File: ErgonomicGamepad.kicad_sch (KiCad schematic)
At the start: 82 parts, among them J1 USB_C_Receptacle_USB2.0_16P, J2 Conn_01x08, J3 Conn_01x08, J4 Conn_01x08, J5 AVR-ISP-6, J6 Conn_01x08, J7 1824417, SW01 SW_DIP_x01, SW02 SW_DIP_x01, SW03 SW_DIP_x01, SW04 SW_DIP_x01, SW05 SW_DIP_x01, SW06 SW_DIP_x01, SW07 SW_DIP_x01, SW08 SW_DIP_x01, SW09 SW_DIP_x01, SW10 SW_DIP_x01, SW11 SW_DIP_x01, SW12 SW_DIP_x01, SW13 SW_DIP_x01, SW14 SW_DIP_x01, SW15 SW_DIP_x01, SW16 SW_DIP_x01, SW17 SW_DIP_x01, SW18 SW_DIP_x01, SW19 SW_DIP_x01, SW20 SW_DIP_x01, SW21 SW_DIP_x01, SW22 SW_DIP_x01, SW23 SW_DIP_x01, SW24 SW_DIP_x01, U1 ATmega32U4-A, U2 USBLC6-2SC6, Y1 Crystal

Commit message: schematic+pcb: mark JP1/TP1-TP7 as DNP and not real parts
JP1 (solder jumper) and TP1-TP7 (test points) are bare PCB pads, not
sourced components, so mark them Do Not Populate and excluded from
BOM, and drop the empty Datasheet field (Manufacturer/MPN/Supplier/
LCSC were never set on these). PCB updated from schematic to match.

Co-Authored-By: Claude Sonnet 5 <noreply@anthropic.com>
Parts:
- JP1: now not fitted
- TP1, TP2, TP3, TP4, TP5, TP6, TP7: now not fitted; now left out of the parts list
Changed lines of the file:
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@@
 		(on_board yes)
 		(in_pos_files yes)
-		(dnp no)
+		(dnp yes)
 		(fields_autoplaced yes)
 		(property "Reference" "JP1"
@@
 			)
 		)
-		(property "Datasheet" ""
-			(at 62.23 52.07 0)
-			(hide yes)
-			(show_name no)
-			(do_not_autoplace no)
-			(effects
-				(font
-					(size 1.27 1.27)
-				)
-			)
-		)
 		(property "Description" "Solder Jumper, 2-pole, open"
 			(at 59.69 52.07 0)
@@
 		(body_style 1)
 		(exclude_from_sim no)
-		(in_bom yes)
+		(in_bom no)
 		(on_board yes)
 		(in_pos_files yes)
-		(dnp no)
+		(dnp yes)
 		(fields_autoplaced yes)
 		(property "Reference" "TP4"
@@
 			)
 		)
-		(property "Datasheet" ""
-			(at 76.2 102.87 0)
-			(hide yes)
-			(show_name no)
-			(do_not_autoplace no)
-			(effects
-				(font
-					(size 1.27 1.27)
-				)
-			)
-		)
 		(property "Description" "test point"
 			(at 81.28 102.87 0)
@@
 		(body_style 1)
 		(exclude_from_sim no)
-		(in_bom yes)
+		(in_bom no)
 		(on_board yes)
 		(in_pos_files yes)
-		(dnp no)
+		(dnp yes)
 		(fields_autoplaced yes)
 		(property "Reference" "TP6"
@@
 			)
 		)
-		(property "Datasheet" ""
-			(at 83.82 80.01 0)
-			(hide yes)
-			(show_name no)
-			(do_not_autoplace no)
-			(effects
-				(font
-					(size 1.27 1.27)
-				)
-			)
-		)
 		(property "Description" "test point"
 			(at 88.9 80.01 0)
@@
 		(body_style 1)
 		(exclude_from_sim no)
-		(in_bom yes)
+		(in_bom no)
 		(on_board yes)
 		(in_pos_files yes)
-		(dnp no)
+		(dnp yes)
 		(fields_autoplaced yes)
 		(property "Reference" "TP5"
@@
 			)
 		)
-		(property "Datasheet" ""
-			(at 93.98 69.85 0)
-			(hide yes)
-			(show_name no)
-			(do_not_autoplace no)
-			(effects
-				(font
-					(size 1.27 1.27)
-				)
-			)
-		)
 		(property "Description" "test point"
 			(at 88.9 69.85 0)
@@
 		(body_style 1)
 		(exclude_from_sim no)
-		(in_bom yes)
+		(in_bom no)
 		(on_board yes)
 		(in_pos_files yes)
-		(dnp no)
+		(dnp yes)
 		(fields_autoplaced yes)
 		(property "Reference" "TP1"
@@
 			)
 		)
-		(property "Datasheet" ""
-			(at 52.07 66.04 0)
-			(hide yes)
-			(show_name no)
-			(do_not_autoplace no)
-			(effects
-				(font
-					(size 1.27 1.27)
-				)
-			)
-		)
 		(property "Description" "test point"
 			(at 52.07 71.12 0)
@@
 		(body_style 1)
 		(exclude_from_sim no)
-		(in_bom yes)
+		(in_bom no)
 		(on_board yes)
 		(in_pos_files yes)
-		(dnp no)
+		(dnp yes)
 		(fields_autoplaced yes)
 		(property "Reference" "TP2"
@@
 			)
 		)
-		(property "Datasheet" ""
-			(at 22.86 53.34 0)
-			(hide yes)
-			(show_name no)
-			(do_not_autoplace no)
-			(effects
-				(font
-					(size 1.27 1.27)
-				)
-			)
-		)
 		(property "Description" "test point"
 			(at 22.86 58.42 0)
@@
 		(body_style 1)
 		(exclude_from_sim no)
-		(in_bom yes)
+		(in_bom no)
 		(on_board yes)
 		(in_pos_files yes)
-		(dnp no)
+		(dnp yes)
 		(fields_autoplaced yes)
 		(property "Reference" "TP3"
@@
 			)
 		)
-		(property "Datasheet" ""
-			(at 86.36 95.25 0)
-			(hide yes)
-			(show_name no)
-			(do_not_autoplace no)
-			(effects
-				(font
-					(size 1.27 1.27)
-				)
-			)
-		)
 		(property "Description" "test point"
 			(at 81.28 95.25 0)
@@
 		(body_style 1)
 		(exclude_from_sim no)
-		(in_bom yes)
+		(in_bom no)
 		(on_board yes)
 		(in_pos_files yes)
-		(dnp no)
+		(dnp yes)
 		(fields_autoplaced yes)
 		(property "Reference" "TP7"
@@
 			(at 76.2 55.88 0)
 			(hide yes)
-			(show_name no)
-			(do_not_autoplace no)
-			(effects
-				(font
-					(size 1.27 1.27)
-				)
-			)
-		)
-		(property "Datasheet" ""
-			(at 76.2 55.88 0)
-			(hide yes)

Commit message: schematic+pcb: rename D25/D26 to LED1/LED2, specify parts
Rename the power and debug indicator LEDs to LED1/LED2 for clarity.
Backfill Manufacturer/MPN/LCSC/Datasheet: LED1 (Pwr, green) with
YONGYUTAI YLED0603G (LCSC C19273151), LED2 (Dbg, red) with Hubei
KENTO Elec KT-0603R (LCSC C2286). PCB updated from schematic to match.

Co-Authored-By: Claude Sonnet 5 <noreply@anthropic.com>
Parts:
- LED1: renamed from D25; LCSC (none) -> C19273151; MPN (none) -> YLED0603G; Manufacturer (none) -> YONGYUTAI
- LED2: renamed from D26; LCSC (none) -> C2286; MPN (none) -> KT-0603R; Manufacturer (none) -> Hubei KENTO Elec
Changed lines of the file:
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@@
 		(in_pos_files yes)
 		(dnp no)
-		(property "Reference" "D25"
+		(property "Reference" "LED1"
 			(at 157.988 152.4 0)
 			(show_name no)
@@
 			)
 		)
-		(property "Datasheet" ""
+		(property "Datasheet" "https://www.lcsc.com/datasheet/C19273151.pdf"
 			(at 157.48 157.48 0)
 			(hide yes)
@@
 			)
 		)
-		(property "Manufacturer" ""
+		(property "Manufacturer" "YONGYUTAI"
 			(at 157.48 157.48 0)
 			(hide yes)
@@
 			)
 		)
-		(property "MPN" ""
+		(property "MPN" "YLED0603G"
 			(at 157.48 157.48 0)
 			(hide yes)
@@
 			)
 		)
-		(property "LCSC" ""
+		(property "LCSC" "C19273151"
 			(at 157.48 157.48 0)
 			(hide yes)
@@
 			(project "ErgonomicGamepad"
 				(path "/c260e742-1838-4e17-a552-9a0d399dd921"
-					(reference "D25")
+					(reference "LED1")
 					(unit 1)
 				)
@@
 		(in_pos_files yes)
 		(dnp no)
-		(property "Reference" "D26"
+		(property "Reference" "LED2"
 			(at 157.988 160.02 0)
 			(show_name no)
@@
 			)
 		)
-		(property "Datasheet" ""
+		(property "Datasheet" "https://www.lcsc.com/datasheet/C2286.pdf"
 			(at 157.48 165.1 0)
 			(hide yes)
@@
 			)
 		)
-		(property "Manufacturer" ""
+		(property "Manufacturer" "Hubei KENTO Elec"
 			(at 157.48 165.1 0)
 			(hide yes)
@@
 			)
 		)
-		(property "MPN" ""
+		(property "MPN" "KT-0603R"
 			(at 157.48 165.1 0)
 			(hide yes)
@@
 			)
 		)
-		(property "LCSC" ""
+		(property "LCSC" "C2286"
 			(at 157.48 165.1 0)
 			(hide yes)
@@
 			(project "ErgonomicGamepad"
 				(path "/c260e742-1838-4e17-a552-9a0d399dd921"
-					(reference "D26")
+					(reference "LED2")
 					(unit 1)
 				)

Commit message: schematic+pcb: confirm U2 ESD part, add JP2 hardware bootloader jumper
U2 (USBLC6-2SC6): backfill LCSC C7519 and switch to LCSC-hosted
datasheet; verified via netlist trace that it's correctly wired to
the USB-C D+/D-/VBUS lines, confirming it's the right part for this
circuit.

JP1: convert from a solder jumper to a real 2-pin header
(Connector_PinHeader_2.54mm, Ckmtw B-2100S02P-A110 / LCSC C124375)
so a physical shunt can be inserted/removed by hand; flip it back to
a populated, in-BOM part.

JP2 (new): same physical-jumper header, wired to U1 pin 33
(PE2/HWB) and GND, so bridging it forces the ATmega32U4's hardware
DFU bootloader on reset. R8 (new, 10k) pulls PE2/HWB up to +5V so
the pin reads a clean high when JP2 isn't bridged, mirroring the
existing RESET/R3/SWR1 pattern.

Connectivity verified via netlist re-export and ERC (0
errors/warnings), including a scratch-copy test simulating both
jumpers bridged. Positions of JP2/R8 were manually adjusted in KiCad
after initial placement; PCB updated to match.

README updated: corrected the stale JP1 footprint entry and added a
note on sourcing 2.54mm jumper shunt caps (LCSC C5305), since JLCPCB
assembly solders the headers but not the removable shunts.

Co-Authored-By: Claude Sonnet 5 <noreply@anthropic.com>
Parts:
- added JP2: Jumper_2_Open, Connector_PinHeader_2.54mm:PinHeader_1x02_P2.54mm_Vertical, symbol Jumper:Jumper_2_Open
- added R8: 10k, Resistor_SMD:R_0603_1608Metric, symbol Device:R
- JP1: value SolderJumper_2_Open -> Jumper_2_Open; footprint Jumper:SolderJumper-2_P1.3mm_Open_Pad1.0x1.5mm -> Connector_PinHeader_2.54mm:PinHeader_1x02_P2.54mm_Vertical; symbol Jumper:SolderJumper_2_Open -> Jumper:Jumper_2_Open; LCSC (none) -> C124375; MPN (none) -> B-2100S02P-A110; Manufacturer (none) -> Ckmtw; Supplier (none) -> LCSC; now fitted; now in the parts list
- U2: LCSC (none) -> C7519
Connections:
- net +5V: now also R8.1
- net GND: now also JP2.2 (B)
- net HWB: now reaches U1.33 (~{HWB}/PE2)
- net HWB: now also JP2.1 (A), R8.2
- no-connect marks 18 -> 17

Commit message: schematic+pcb: specify U1 (ATmega32U4-AU) part data
Backfill Manufacturer (Microchip), MPN (ATMEGA32U4-AU), and LCSC
(C44854), and switch the datasheet link to LCSC's hosted copy.
Picked the plain -AU variant over -AUR (reel) for better stock
(1,356 vs 24 units), same TQFP-44 package matching the footprint
already in use.

Co-Authored-By: Claude Sonnet 5 <noreply@anthropic.com>
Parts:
- U1: LCSC (none) -> C44854; MPN (none) -> ATMEGA32U4-AU; Manufacturer (none) -> Microchip
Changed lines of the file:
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@@
 			)
 		)
-		(property "Datasheet" "http://ww1.microchip.com/downloads/en/DeviceDoc/Atmel-7766-8-bit-AVR-ATmega16U4-32U4_Datasheet.pdf"
+		(property "Datasheet" "https://www.lcsc.com/datasheet/C44854.pdf"
 			(at 115.57 147.32 0)
 			(hide yes)
@@
 			)
 		)
-		(property "Manufacturer" ""
+		(property "Manufacturer" "Microchip"
 			(at 115.57 147.32 0)
 			(hide yes)
@@
 			)
 		)
-		(property "MPN" ""
+		(property "MPN" "ATMEGA32U4-AU"
 			(at 115.57 147.32 0)
 			(hide yes)
@@
 			)
 		)
-		(property "LCSC" ""
+		(property "LCSC" "C44854"
 			(at 115.57 147.32 0)
 			(hide yes)

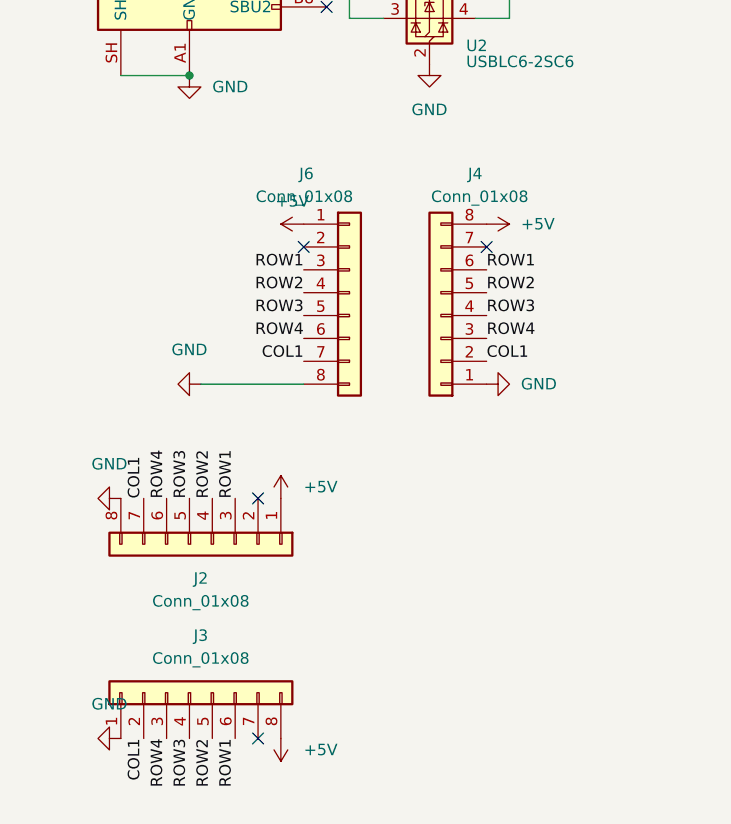
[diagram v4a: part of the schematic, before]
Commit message: schematic+pcb: specify J2/J3/J4/J6 headers, match connector pinouts
Backfill Manufacturer (Ckmtw), MPN (B-2100S08P-A110), LCSC (C124381),
and datasheet for the J2/J3/J4/J6 edge-connector headers - confirmed
through-hole (thru_hole pads), matching the existing vertical
PinHeader footprint.

Reorient all four connectors to a consistent, matched pin-to-signal
mapping (ROW1-4 on pins 3-6, COL1 on pin 7 across all of them,
previously J4/J6 were mirrored relative to J2/J3) so a standard
straight ribbon cable works without needing a reversed/twisted crimp.
Verified via netlist export and a clean ERC pass.

Co-Authored-By: Claude Sonnet 5 <noreply@anthropic.com>
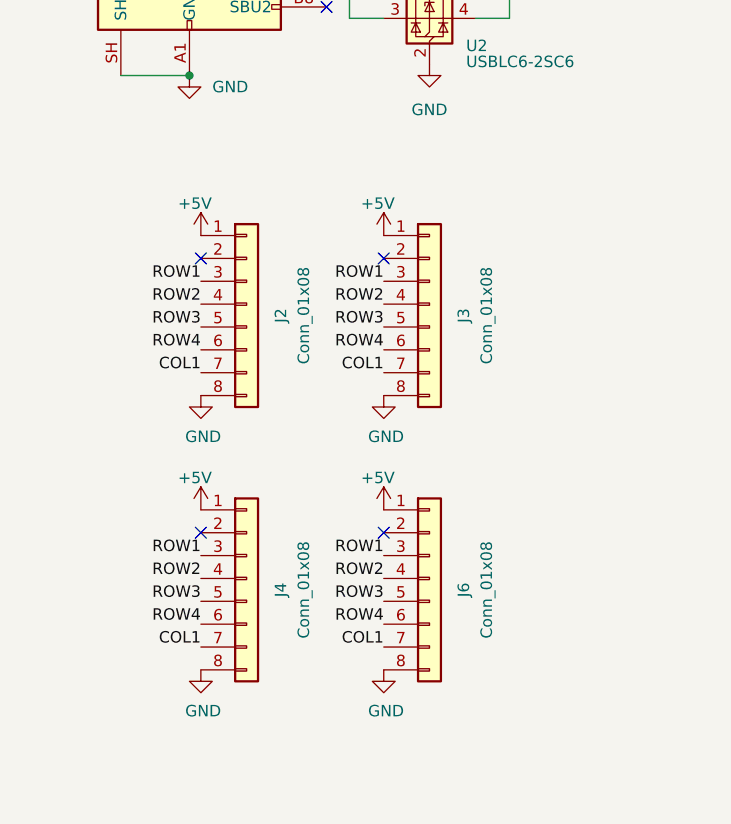
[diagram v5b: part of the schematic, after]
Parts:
- J2, J3, J4, J6: LCSC (none) -> C124381; MPN (none) -> B-2100S08P-A110; Manufacturer (none) -> Ckmtw
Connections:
- net +5V: now also J3.1 (Pin_1), J4.1 (Pin_1); no longer J3.8 (Pin_8), J4.8 (Pin_8)
- net COL1: now also J3.7 (Pin_7), J4.7 (Pin_7); no longer J3.2 (Pin_2), J4.2 (Pin_2)
- net GND: now also J3.8 (Pin_8), J4.8 (Pin_8); no longer J3.1 (Pin_1), J4.1 (Pin_1)
- net ROW1: now also J3.3 (Pin_3), J4.3 (Pin_3); no longer J3.6 (Pin_6), J4.6 (Pin_6)
- net ROW2: now also J3.4 (Pin_4), J4.4 (Pin_4); no longer J3.5 (Pin_5), J4.5 (Pin_5)
- net ROW3: now also J3.5 (Pin_5), J4.5 (Pin_5); no longer J3.4 (Pin_4), J4.4 (Pin_4)
- net ROW4: now also J3.6 (Pin_6), J4.6 (Pin_6); no longer J3.3 (Pin_3), J4.3 (Pin_3)
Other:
- moved on the sheet: J2

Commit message: schematic: specify R1-R8 resistor parts
Backfill Manufacturer, MPN, LCSC, and datasheet for all eight
resistors using YAGEO's RC0603FR-07 series throughout for BOM
consistency, matching the existing 0603 footprint:

- R1/R2 (20R): RC0603FR-0720RL, LCSC C125758
- R3/R8 (10k): RC0603FR-0710KL, LCSC C98220
- R4/R5 (5.1k): RC0603FR-075K1L, LCSC C105580
- R6 (1k): RC0603FR-071KL, LCSC C22548
- R7 (330): RC0603FR-07330RL, LCSC C105881

Co-Authored-By: Claude Sonnet 5 <noreply@anthropic.com>
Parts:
- R1, R2: LCSC (none) -> C125758; MPN (none) -> RC0603FR-0720RL; Manufacturer (none) -> YAGEO
- R3, R8: LCSC (none) -> C98220; MPN (none) -> RC0603FR-0710KL; Manufacturer (none) -> YAGEO
- R4, R5: LCSC (none) -> C105580; MPN (none) -> RC0603FR-075K1L; Manufacturer (none) -> YAGEO
- R6: LCSC (none) -> C22548; MPN (none) -> RC0603FR-071KL; Manufacturer (none) -> YAGEO
- R7: LCSC (none) -> C105881; MPN (none) -> RC0603FR-07330RL; Manufacturer (none) -> YAGEO
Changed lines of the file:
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@@
 			)
 		)
-		(property "Datasheet" ""
+		(property "Datasheet" "https://www.lcsc.com/datasheet/C105580.pdf"
 			(at 52.07 92.71 0)
 			(hide yes)
@@
 			)
 		)
-		(property "Manufacturer" ""
+		(property "Manufacturer" "YAGEO"
 			(at 52.07 92.71 90)
 			(hide yes)
@@
 			)
 		)
-		(property "MPN" ""
+		(property "MPN" "RC0603FR-075K1L"
 			(at 52.07 92.71 90)
 			(hide yes)
@@
 			)
 		)
-		(property "LCSC" ""
+		(property "LCSC" "C105580"
 			(at 52.07 92.71 90)
 			(hide yes)
@@
 			)
 		)
-		(property "Datasheet" ""
+		(property "Datasheet" "https://www.lcsc.com/datasheet/C22548.pdf"
 			(at 146.05 157.48 0)
 			(hide yes)
@@
 			)
 		)
-		(property "Manufacturer" ""
+		(property "Manufacturer" "YAGEO"
 			(at 146.05 157.48 90)
 			(hide yes)
@@
 			)
 		)
-		(property "MPN" ""
+		(property "MPN" "RC0603FR-071KL"
 			(at 146.05 157.48 90)
 			(hide yes)
@@
 			)
 		)
-		(property "LCSC" ""
+		(property "LCSC" "C22548"
 			(at 146.05 157.48 90)
 			(hide yes)
@@
 			)
 		)
-		(property "Datasheet" ""
+		(property "Datasheet" "https://www.lcsc.com/datasheet/C105580.pdf"
 			(at 52.07 87.63 0)
 			(hide yes)
@@
 			)
 		)
-		(property "Manufacturer" ""
+		(property "Manufacturer" "YAGEO"
 			(at 52.07 87.63 90)
 			(hide yes)
@@
 			)
 		)
-		(property "MPN" ""
+		(property "MPN" "RC0603FR-075K1L"
 			(at 52.07 87.63 90)
 			(hide yes)
@@
 			)
 		)
-		(property "LCSC" ""
+		(property "LCSC" "C105580"
 			(at 52.07 87.63 90)
 			(hide yes)
@@
 			)
 		)
-		(property "Datasheet" ""
+		(property "Datasheet" "https://www.lcsc.com/datasheet/C125758.pdf"
 			(at 72.39 102.87 0)
 			(hide yes)
@@
 			)
 		)
-		(property "Manufacturer" ""
+		(property "Manufacturer" "YAGEO"
 			(at 72.39 102.87 90)
 			(hide yes)
@@
 			)
 		)
-		(property "MPN" ""
+		(property "MPN" "RC0603FR-0720RL"
 			(at 72.39 102.87 90)
 			(hide yes)
@@
 			)
 		)
-		(property "LCSC" ""
+		(property "LCSC" "C125758"
 			(at 72.39 102.87 90)
 			(hide yes)
@@
 			)
 		)
-		(property "Datasheet" ""
+		(property "Datasheet" "https://www.lcsc.com/datasheet/C98220.pdf"
 			(at 73.66 43.18 0)
 			(hide yes)
@@
 			)
 		)
-		(property "Manufacturer" ""
+		(property "Manufacturer" "YAGEO"
 			(at 73.66 43.18 0)
 			(hide yes)
@@
 			)
 		)
-		(property "MPN" ""
+		(property "MPN" "RC0603FR-0710KL"
 			(at 73.66 43.18 0)
 			(hide yes)
@@
 			)
 		)
-		(property "LCSC" ""
+		(property "LCSC" "C98220"
 			(at 73.66 43.18 0)
 			(hide yes)
@@
 			)
 		)
-		(property "Datasheet" ""
+		(property "Datasheet" "https://www.lcsc.com/datasheet/C125758.pdf"
 			(at 72.39 97.79 0)
 			(hide yes)
@@
 			)
 		)
-		(property "Manufacturer" ""
+		(property "Manufacturer" "YAGEO"
 			(at 72.39 97.79 0)
 			(hide yes)
@@
 			)
 		)
-		(property "MPN" ""
+		(property "MPN" "RC0603FR-0720RL"
 			(at 72.39 97.79 0)
 			(hide yes)
@@
 			)
 		)
-		(property "LCSC" ""
+		(property "LCSC" "C125758"
 			(at 72.39 97.79 0)
 			(hide yes)
@@
 			)
 		)
-		(property "Datasheet" ""
+		(property "Datasheet" "https://www.lcsc.com/datasheet/C98220.pdf"
 			(at 152.4 36.83 0)
 			(hide yes)
@@
 			)
 		)
-		(property "Manufacturer" ""
+		(property "Manufacturer" "YAGEO"
 			(at 152.4 36.83 0)
 			(hide yes)
@@
 			)
 		)
-		(property "MPN" ""
+		(property "MPN" "RC0603FR-0710KL"
 			(at 152.4 36.83 0)
 			(hide yes)
@@
 			)
 		)
-		(property "LCSC" ""
+		(property "LCSC" "C98220"
 			(at 152.4 36.83 0)
 			(hide yes)
@@
 			)
 		)
-		(property "Datasheet" ""
+		(property "Datasheet" "https://www.lcsc.com/datasheet/C105881.pdf"
 			(at 146.05 165.1 0)
 			(hide yes)
@@
 			)
 		)
-		(property "Manufacturer" ""
+		(property "Manufacturer" "YAGEO"
 			(at 146.05 165.1 0)
 			(hide yes)
@@
 			)
 		)
-		(property "MPN" ""
+		(property "MPN" "RC0603FR-07330RL"
 			(at 146.05 165.1 0)
 			(hide yes)
@@
 			)
 		)
-		(property "LCSC" ""
+		(property "LCSC" "C105881"
 			(at 146.05 165.1 0)
 			(hide yes)

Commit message: schematic: specify C1-C5 capacitor parts
Backfill Manufacturer, MPN, LCSC, and datasheet for all five
capacitors using YAGEO parts matching the existing 0603 footprint:

- C1/C2 (22pF): CC0603JRNPO8BN220, LCSC C519390, NP0/C0G dielectric
  (stable temperature coefficient, appropriate for crystal load caps)
- C3 (1uF): CC0603KRX5R7BB105, LCSC C106215, X5R
- C4 (4.7uF): CC0603KRX5R6BB475, LCSC C109456, X5R
- C5 (100nF): CC0603KRX7R9BB104, LCSC C14663, X7R

Co-Authored-By: Claude Sonnet 5 <noreply@anthropic.com>
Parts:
- C1, C2: LCSC (none) -> C519390; MPN (none) -> CC0603JRNPO8BN220; Manufacturer (none) -> YAGEO
- C3: LCSC (none) -> C106215; MPN (none) -> CC0603KRX5R7BB105; Manufacturer (none) -> YAGEO
- C4: LCSC (none) -> C109456; MPN (none) -> CC0603KRX5R6BB475; Manufacturer (none) -> YAGEO
- C5: LCSC (none) -> C14663; MPN (none) -> CC0603KRX7R9BB104; Manufacturer (none) -> YAGEO
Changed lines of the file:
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@@
 			)
 		)
-		(property "Datasheet" ""
+		(property "Datasheet" "https://www.lcsc.com/datasheet/C109456.pdf"
 			(at 26.67 54.61 0)
 			(hide yes)
@@
 			)
 		)
-		(property "Manufacturer" ""
+		(property "Manufacturer" "YAGEO"
 			(at 26.67 54.61 0)
 			(hide yes)
@@
 			)
 		)
-		(property "MPN" ""
+		(property "MPN" "CC0603KRX5R6BB475"
 			(at 26.67 54.61 0)
 			(hide yes)
@@
 			)
 		)
-		(property "LCSC" ""
+		(property "LCSC" "C109456"
 			(at 26.67 54.61 0)
 			(hide yes)
@@
 			)
 		)
-		(property "Datasheet" ""
+		(property "Datasheet" "https://www.lcsc.com/datasheet/C519390.pdf"
 			(at 72.39 80.01 0)
 			(hide yes)
@@
 			)
 		)
-		(property "Manufacturer" ""
+		(property "Manufacturer" "YAGEO"
 			(at 72.39 80.01 0)
 			(hide yes)
@@
 			)
 		)
-		(property "MPN" ""
+		(property "MPN" "CC0603JRNPO8BN220"
 			(at 72.39 80.01 0)
 			(hide yes)
@@
 			)
 		)
-		(property "LCSC" ""
+		(property "LCSC" "C519390"
 			(at 72.39 80.01 0)
 			(hide yes)
@@
 			)
 		)
-		(property "Datasheet" ""
+		(property "Datasheet" "https://www.lcsc.com/datasheet/C519390.pdf"
 			(at 72.39 72.39 0)
 			(hide yes)
@@
 			)
 		)
-		(property "Manufacturer" ""
+		(property "Manufacturer" "YAGEO"
 			(at 72.39 72.39 0)
 			(hide yes)
@@
 			)
 		)
-		(property "MPN" ""
+		(property "MPN" "CC0603JRNPO8BN220"
 			(at 72.39 72.39 0)
 			(hide yes)
@@
 			)
 		)
-		(property "LCSC" ""
+		(property "LCSC" "C519390"
 			(at 72.39 72.39 0)
 			(hide yes)
@@
 			)
 		)
-		(property "Datasheet" ""
+		(property "Datasheet" "https://www.lcsc.com/datasheet/C106215.pdf"
 			(at 68.58 63.5 0)
 			(hide yes)
@@
 			)
 		)
-		(property "Manufacturer" ""
+		(property "Manufacturer" "YAGEO"
 			(at 68.58 63.5 0)
 			(hide yes)
@@
 			)
 		)
-		(property "MPN" ""
+		(property "MPN" "CC0603KRX5R7BB105"
 			(at 68.58 63.5 0)
 			(hide yes)
@@
 			)
 		)
-		(property "LCSC" ""
+		(property "LCSC" "C106215"
 			(at 68.58 63.5 0)
 			(hide yes)
@@
 			)
 		)
-		(property "Datasheet" ""
+		(property "Datasheet" "https://www.lcsc.com/datasheet/C14663.pdf"
 			(at 41.91 54.61 0)
 			(hide yes)
@@
 			)
 		)
-		(property "Manufacturer" ""
+		(property "Manufacturer" "YAGEO"
 			(at 41.91 54.61 0)
 			(hide yes)
@@
 			)
 		)
-		(property "MPN" ""
+		(property "MPN" "CC0603KRX7R9BB104"
 			(at 41.91 54.61 0)
 			(hide yes)
@@
 			)
 		)
-		(property "LCSC" ""
+		(property "LCSC" "C14663"
 			(at 41.91 54.61 0)
 			(hide yes)
